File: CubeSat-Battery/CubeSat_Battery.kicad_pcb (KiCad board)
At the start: 2 copper layers, 92 x 92 mm, 4 parts, among them J1 Conn_01x02_Pin, U1 BatteryPack

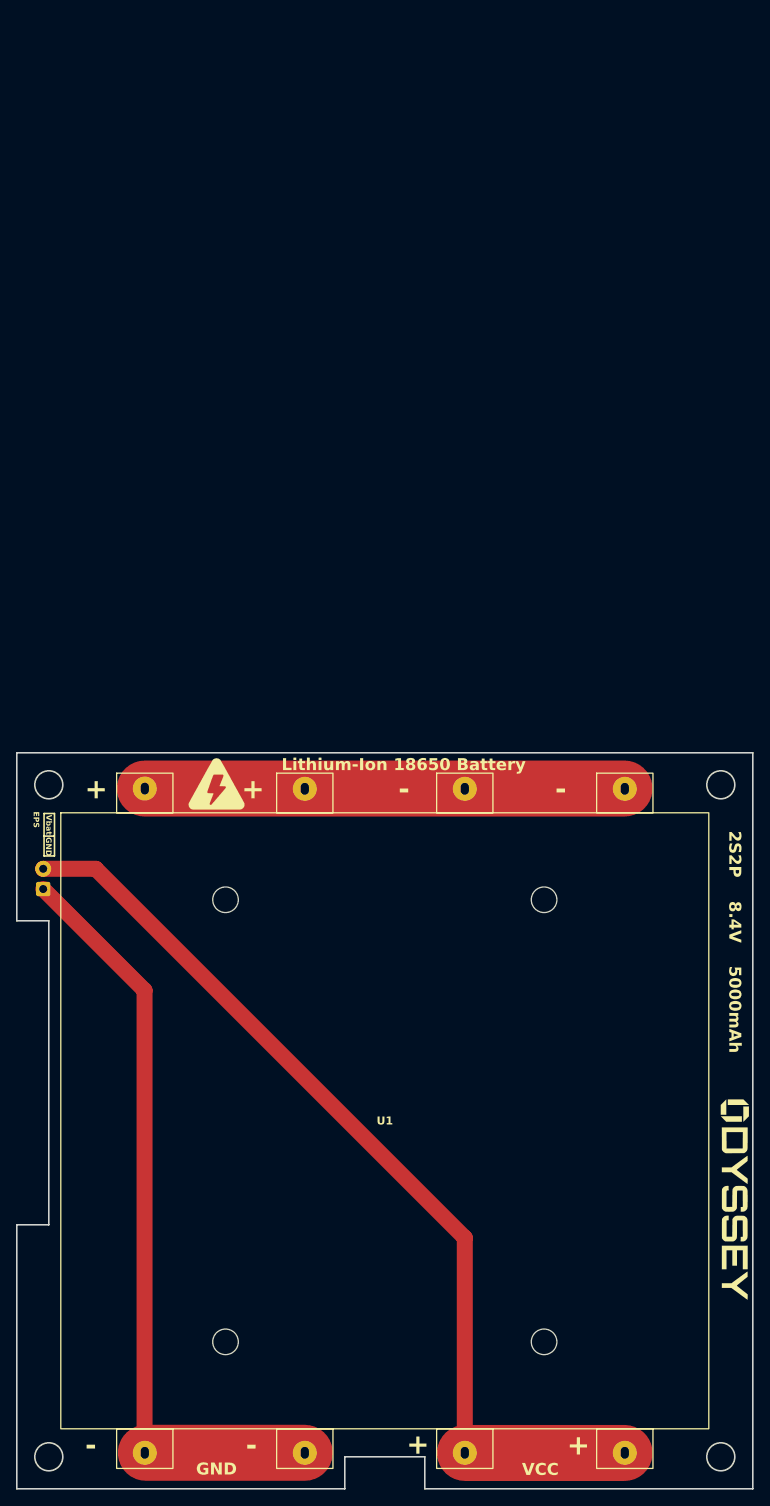
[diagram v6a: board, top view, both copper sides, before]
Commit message: new origin placement
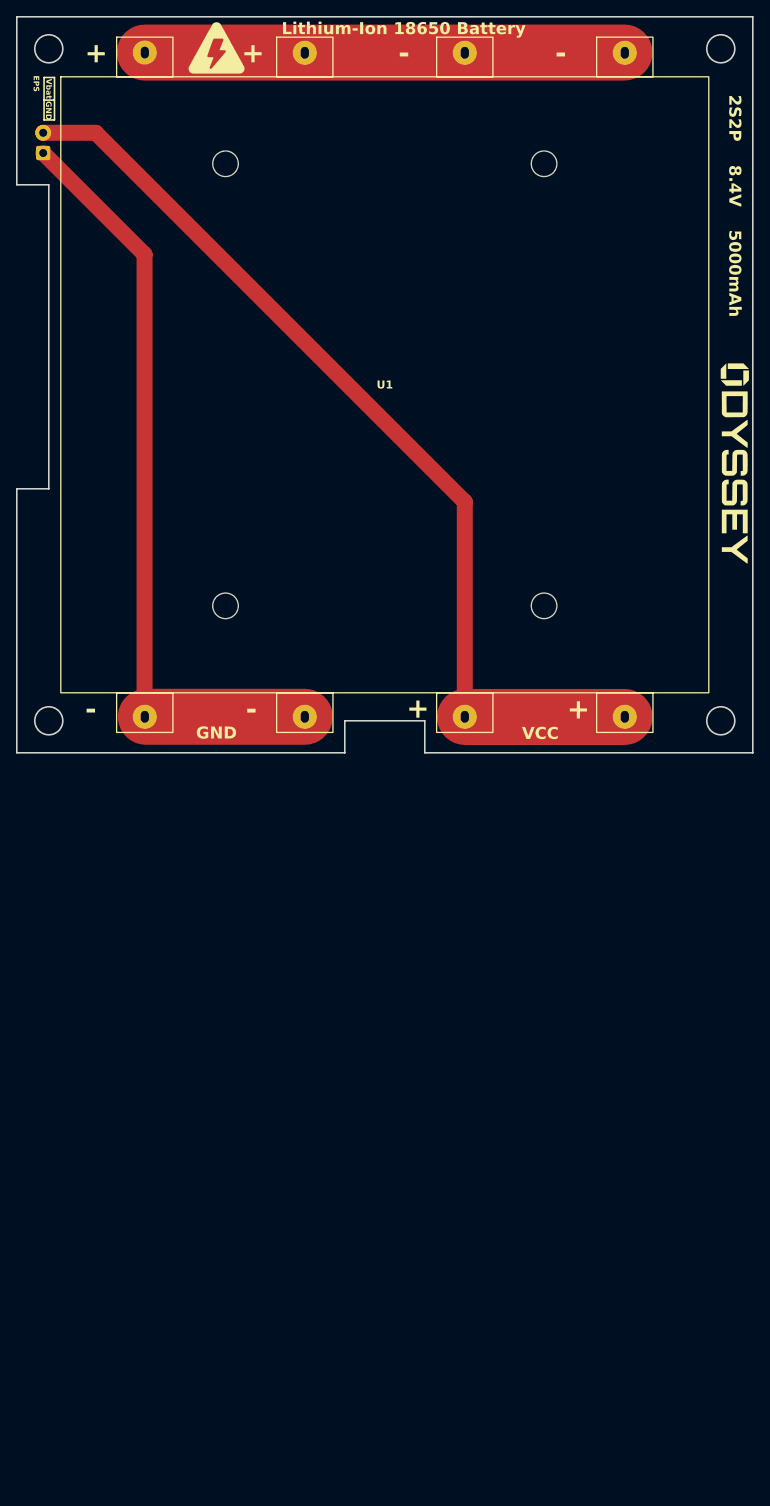
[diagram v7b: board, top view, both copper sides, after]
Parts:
- moved G*** 92.0 mm to (89.8, -36.1)
- moved G*** 92.0 mm to (25.0, -88.1)
- moved J1 92.0 mm to (3.30, -75.0)
- moved U1 92.0 mm to (46.0, -46.0)

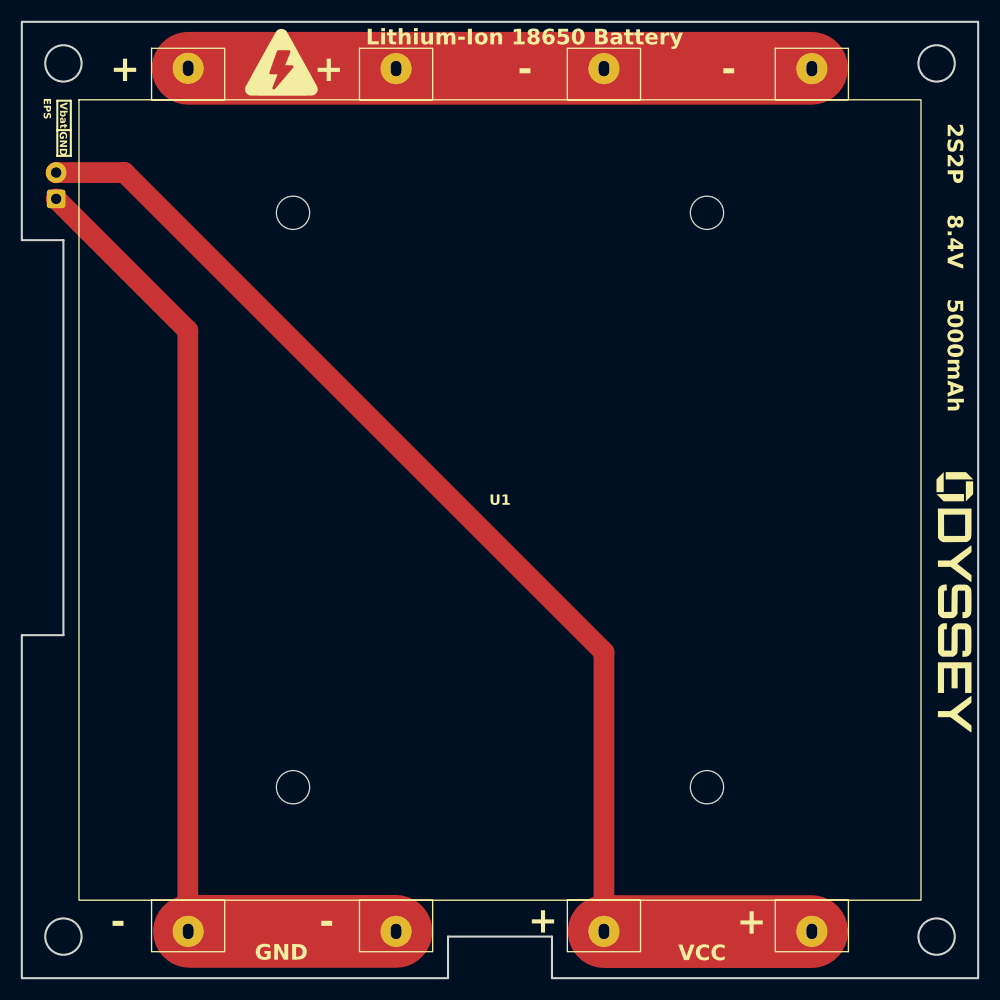
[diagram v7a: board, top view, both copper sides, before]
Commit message: final changes in ALL 3 pcbs: mounting wholes config, and a few connector changes
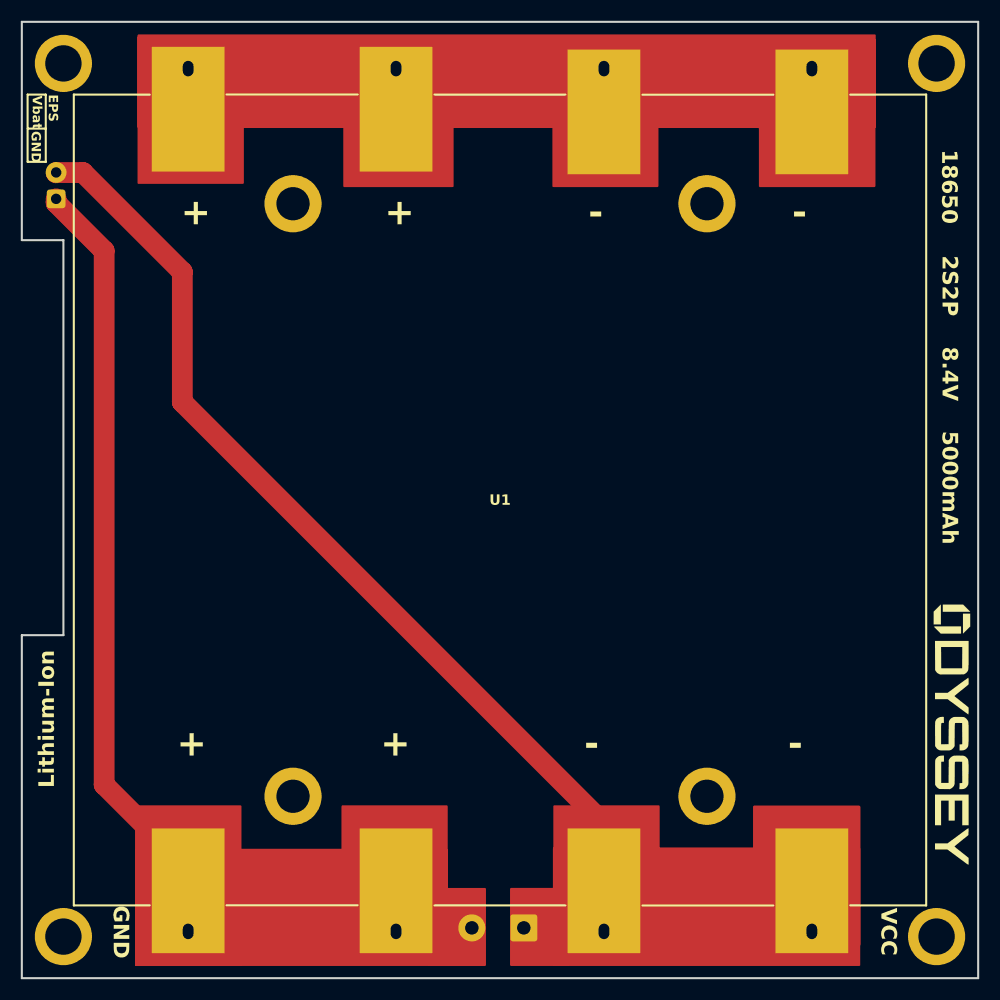
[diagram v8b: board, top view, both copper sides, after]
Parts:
- removed the G*** at (25.0, -88.1)
- added J6: Screw_Terminal_01x02, TerminalBlock_Phoenix:TerminalBlock_Phoenix_MKDS-1,5-2_1x02_P5.00mm_Horizontal, B.Cu at (48.3, -4.84)
- added REF**: MountingHole_3.5mm_Pad, MountingHole:MountingHole_3.5mm_Pad, F.Cu at (4.00, -88.0)
- added REF**: MountingHole_3.5mm_Pad, MountingHole:MountingHole_3.5mm_Pad, F.Cu at (4.00, -4.00)
- added REF**: MountingHole_3.5mm_Pad, MountingHole:MountingHole_3.5mm_Pad, F.Cu at (88.0, -88.0)
- added REF**: MountingHole_3.5mm_Pad, MountingHole:MountingHole_3.5mm_Pad, F.Cu at (88.0, -4.00)
- moved G*** 12.7 mm to (89.5, -23.3)
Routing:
- net Vcell_4.2V: track 60.0 -> 0.00 mm
- net Vbat_8.4V: track 118.8 -> 96.8 mm
- net GND: track 95.7 -> 76.2 mm
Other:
- outline, holes or cut-outs redrawn
- board text added: "18650"
- board text added: "Lithium-Ion"
- board text removed: "Lithium-Ion 18650 Battery"
